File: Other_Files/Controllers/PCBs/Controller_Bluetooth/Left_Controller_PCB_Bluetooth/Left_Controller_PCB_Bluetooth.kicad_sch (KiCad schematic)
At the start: 13 parts

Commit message: Updated the Controllers' PCB to version 1.2
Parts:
- H1, H2, H3, H4: footprint MountingHole:MountingHole_3mm -> MountingHole:MountingHole_3.2mm_M3
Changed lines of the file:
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@@
 			)
 		)
-		(property "Footprint" "MountingHole:MountingHole_3mm"
+		(property "Footprint" "MountingHole:MountingHole_3.2mm_M3"
 			(at 101.6 190.5 0)
 			(effects
@@
 			)
 		)
-		(property "Footprint" "MountingHole:MountingHole_3mm"
+		(property "Footprint" "MountingHole:MountingHole_3.2mm_M3"
 			(at 25.4 190.5 0)
 			(effects
@@
 			)
 		)
-		(property "Footprint" "MountingHole:MountingHole_3mm"
+		(property "Footprint" "MountingHole:MountingHole_3.2mm_M3"
 			(at 50.8 190.5 0)
 			(effects
@@
 			)
 		)
-		(property "Footprint" "MountingHole:MountingHole_3mm"
+		(property "Footprint" "MountingHole:MountingHole_3.2mm_M3"
 			(at 76.2 190.5 0)
 			(effects

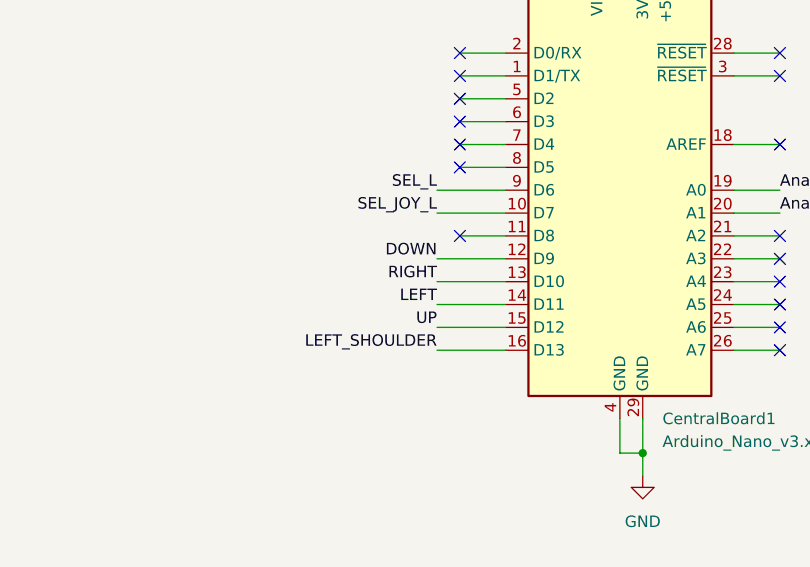
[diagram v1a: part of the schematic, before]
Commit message: Updated Bluetooth Controllers' PCBs
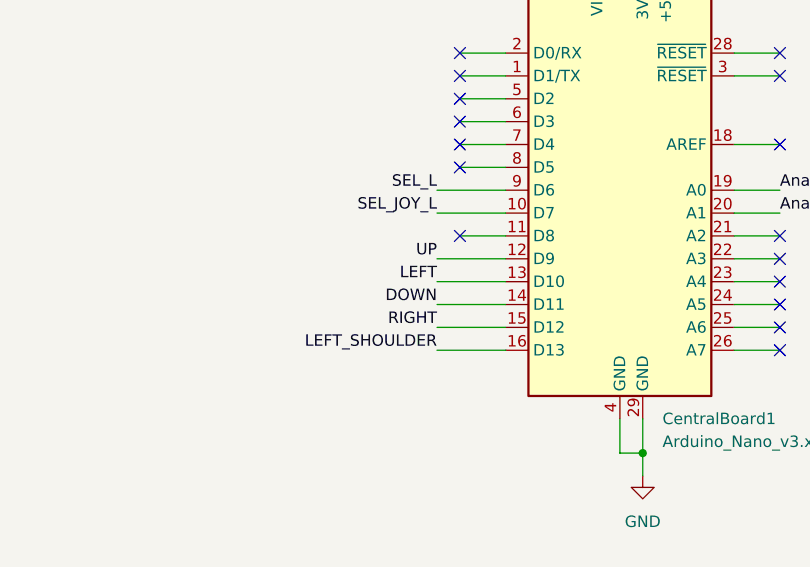
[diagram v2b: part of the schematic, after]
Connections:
- net DOWN: now also CentralBoard1.14 (D11); no longer CentralBoard1.12 (D9)
- net LEFT: now also CentralBoard1.13 (D10); no longer CentralBoard1.14 (D11)
- net RIGHT: now also CentralBoard1.15 (D12); no longer CentralBoard1.13 (D10)
- net UP: now also CentralBoard1.12 (D9); no longer CentralBoard1.15 (D12)
